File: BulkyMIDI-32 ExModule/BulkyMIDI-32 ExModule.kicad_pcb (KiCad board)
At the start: 2 copper layers, 100 x 100 mm, 28 parts, among them J1 DC IN, J2 Wavetable, J3 MIDI IN, J4 AUDIO, J5 MIDI THRU, J6 ExModule_Panel, M1 Mounting, M2 Mounting, M3 Mounting, M4 Mounting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

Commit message: Add activity
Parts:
- added C2: 3.3uF, Capacitor_THT:CP_Radial_D5.0mm_P2.00mm, F.Cu at (222.5, 84.7)
- added C3: 10nF, Capacitor_THT:C_Disc_D4.7mm_W2.5mm_P5.00mm, F.Cu at (196.7, 91.5)
- added C4: 100nF, Capacitor_THT:C_Disc_D4.7mm_W2.5mm_P5.00mm, F.Cu at (196.7, 95.6)
- added FB1: Wired Ferrite, Inductor_THT:L_Axial_L7.0mm_D3.3mm_P10.16mm_Horizontal_Fastron_MICC, F.Cu at (82.5, 110.5)
- added Q1: 2N3906, Package_TO_SOT_THT:TO-92_Inline_Wide, F.Cu at (204.8, 96.5)
- added R1: 100k, resistor:R_Axial_DIN0207_L6.3mm_D2.5mm_P10.16mm_Horizontal, F.Cu at (196.7, 83.4)
- added R2: 10k, resistor:R_Axial_DIN0207_L6.3mm_D2.5mm_P10.16mm_Horizontal, F.Cu at (196.7, 87.5)
- added U2: NE555P, Package_DIP:DIP-8_W7.62mm_Socket_LongPads, F.Cu at (210.5, 83.5)
- moved C1 110.0 mm to (232.1, 88.3), turned to 0 degrees
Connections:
- R5 pad 2: (no net) -> /Activity LED/Activity
- U1 pad 1: GND -> Net-(U1-Pad1)
- U1 pad 10: Net-(U1-Pad10) -> Net-(U1-Pad1)
- U1 pad 13: Net-(U1-Pad10) -> Net-(U1-Pad1)
- U1 pad 2: (no net) -> /Activity LED/MIDI
- U1 pad 9: Net-(U1-Pad10) -> Net-(U1-Pad1)
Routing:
- net Net-(U1-Pad10): track 15.1 -> 0.00 mm
- net Net-(U1-Pad1): track 0.00 -> 15.1 mm

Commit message: ExModule layout
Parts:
- removed SW4: RESET, Button_Switch_THT:SW_Tactile_SPST_Angled_PTS645Vx39-2LFS
- added A1: ExPower, BulkyMIDI-32:ExPower, F.Cu at (88.9, 54.6)
- added C5: 100nF, Capacitor_THT:C_Disc_D4.7mm_W2.5mm_P5.00mm, F.Cu at (163.2, 85.7)
- added C8: 10uF, Capacitor_THT:CP_Radial_D5.0mm_P2.00mm, F.Cu at (165.7, 78.1)
- added C9: 100nF, Capacitor_THT:C_Disc_D4.7mm_W2.5mm_P5.00mm, F.Cu at (148.6, 78.1)
- added G***: LOGO, artwork:BulkyMIDI-32_8bit, F.Cu at (125.1, 99.1)
- added R3: 1M, resistor:R_Axial_DIN0207_L6.3mm_D2.5mm_P10.16mm_Horizontal, F.Cu at (148.6, 86.4)
- added R7: 47k, resistor:R_Axial_DIN0207_L6.3mm_D2.5mm_P10.16mm_Horizontal, F.Cu at (168.3, 89.5)
- added R8: 1k, resistor:R_Axial_DIN0207_L6.3mm_D2.5mm_P10.16mm_Horizontal, F.Cu at (104.8, 74.6)
- added SW1: RESET, Button_Switch_THT:SW_Tactile_SPST_Angled_PTS645Vx39-2LFS, F.Cu at (158.1, 151.8)
- added U4: NE555, Package_DIP:DIP-8_W7.62mm_Socket_LongPads, F.Cu at (152.4, 85.7)
- FB1: footprint Inductor_THT:L_Axial_L7.0mm_D3.3mm_P10.16mm_Horizontal_Fastron_MICC -> BulkyMIDI-32:L_Axial_L7.0mm_D3.3mm_P10.16mm_Horizontal_Fastron_MICC
- moved C1 145.4 mm to (87.0, 79.4), turned to 270 degrees
- moved D4 131.5 mm to (93.3, 73.7), turned to 180 degrees
- moved U2 96.2 mm to (114.3, 85.7), turned to 90 degrees
- moved C4 87.7 mm to (110.5, 79.4), turned to 270 degrees
- moved C2 86.9 mm to (135.9, 78.1)
- moved REF*** 79.4 mm to (120.7, 118.7)
- moved Q1 76.0 mm to (130.2, 81.9), turned to 180 degrees
- moved R2 71.6 mm to (125.1, 86.4)
- moved C3 67.9 mm to (130.1, 78.1), turned to 180 degrees
- moved R1 62.7 mm to (134.0, 83.2)
- moved R19 47.1 mm to (110.5, 59.7), turned to 270 degrees
- moved U1 40.3 mm to (90.8, 85.7)
- moved C6 38.2 mm to (75.6, 76.2)
- moved C7 34.9 mm to (94.6, 61.0)
- moved D3 34.9 mm to (98.4, 70.5)
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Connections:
- J2 pad 18: (no net) -> +12V
- J2 pad 22: (no net) -> -12V
- J2 pad 26: RESET -> ~RESET
- J6 pad 19: RESET -> RESET_SW
- U1 pad 3: GND -> Net-(U1-Pad3)
- U1 pad 4: (no net) -> ~RESET
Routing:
- net +5V: track 8.67 -> 389.2 mm
- net -12V: track 0.00 -> 122.1 mm
- net RESET: track 116.6 -> 0.00 mm
- net RESET_SW: track 0.00 -> 109.1 mm
- net +12V: track 0.00 -> 107.3 mm
- net ~RESET: track 0.00 -> 75.6 mm, vias 0 -> 2
- net Net-(U1-Pad3): track 0.00 -> 67.1 mm
- net /Activity LED/Activity: track 0.00 -> 65.6 mm, vias 0 -> 1
- net MIDI_THRU: track 8.15 -> 65.6 mm
- net /Activity LED/MIDI: track 0.00 -> 45.4 mm
- net MIDI_IN: track 0.00 -> 31.3 mm, vias 0 -> 1
- net Net-(C8-Pad1): track 0.00 -> 27.9 mm
- net Net-(C2-Pad1): track 0.00 -> 27.5 mm
- net Net-(R19-Pad2): track 22.6 -> 40.7 mm
- net Net-(J5-Pad4): track 0.00 -> 17.5 mm
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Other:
- board text added: "+12V"
- board text added: "+5V"
- board text added: "-12V"
- board text added: "AUDIO"
- board text added: "BulkyMIDI-32 ExModule (rev. A) github.com/tebl"
- board text added: "LEFT"
- board text added: "MIDI"
- board text added: "RIGHT"
- board text added: "~RESET"
- board text removed: "BulkyMIDI-32 Play (rev. B) github.com/tebl"
- board text removed: "MICRO SD"

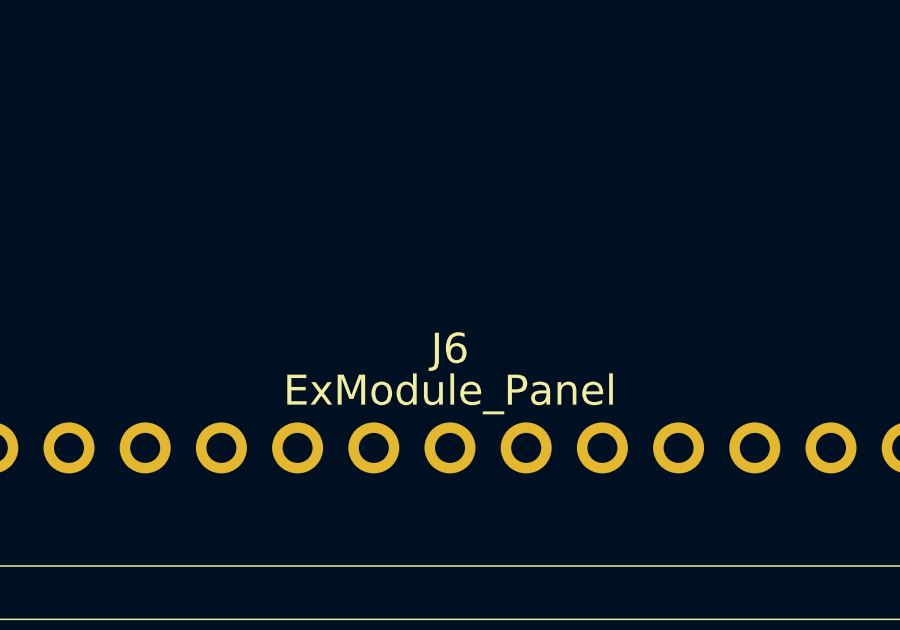
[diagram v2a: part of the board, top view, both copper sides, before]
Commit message: Add ExModule panel
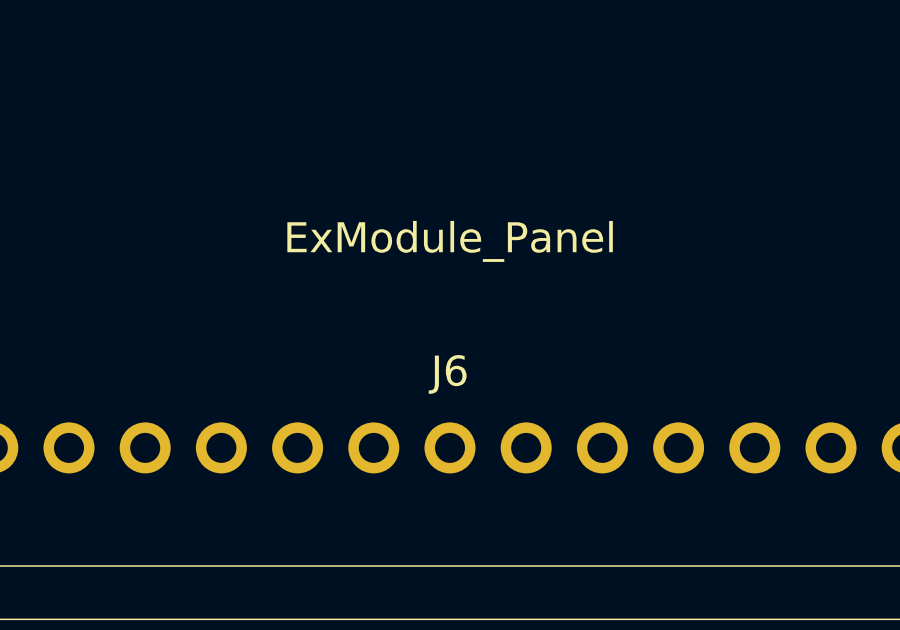
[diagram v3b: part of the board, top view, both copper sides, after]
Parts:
- J6: footprint BulkyMIDI-32:Play_Panel -> BulkyMIDI-32:ExModule_Panel
